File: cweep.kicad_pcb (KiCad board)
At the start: 2 copper layers, 108 x 82.5 mm, 73 parts, among them J1 24AWG Hole, J2 24AWG Hole, SW1 SW_Push, SW10 SW_Push, SW11 SW_Push, SW12 SW_Push, SW13 SW_Push, SW14 SW_Push, SW15 SW_Push, SW16 SW_Push, SW17 SW_Push, SW18 SW_SPST, SW19 SW_Omron_B3FS, SW2 SW_Push, SW3 SW_Push, SW4 SW_Push, SW5 SW_Push, SW6 SW_Push, SW7 SW_Push, SW8 SW_Push, SW9 SW_Push, U1 XIAO-nRF52840, U2 BQ25504RGTR

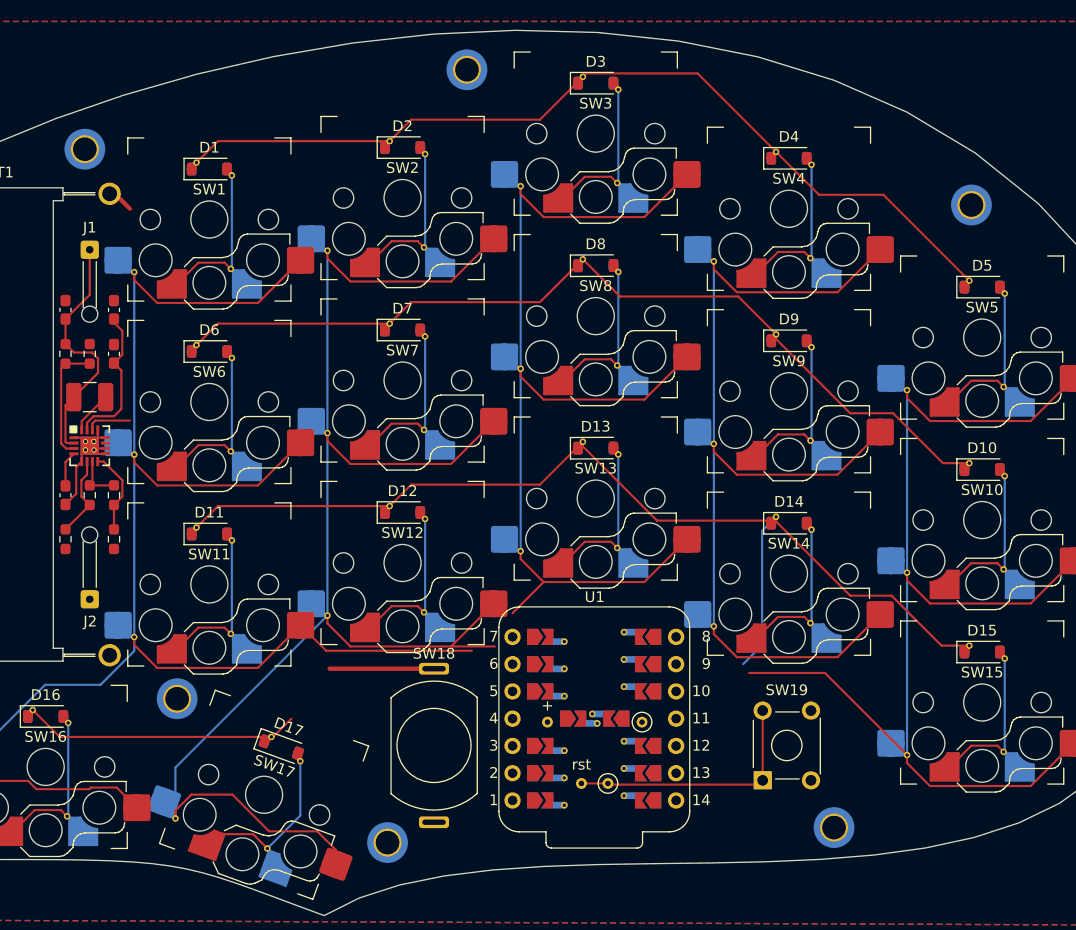
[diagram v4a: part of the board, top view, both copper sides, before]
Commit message: feat: make remaining components reversible
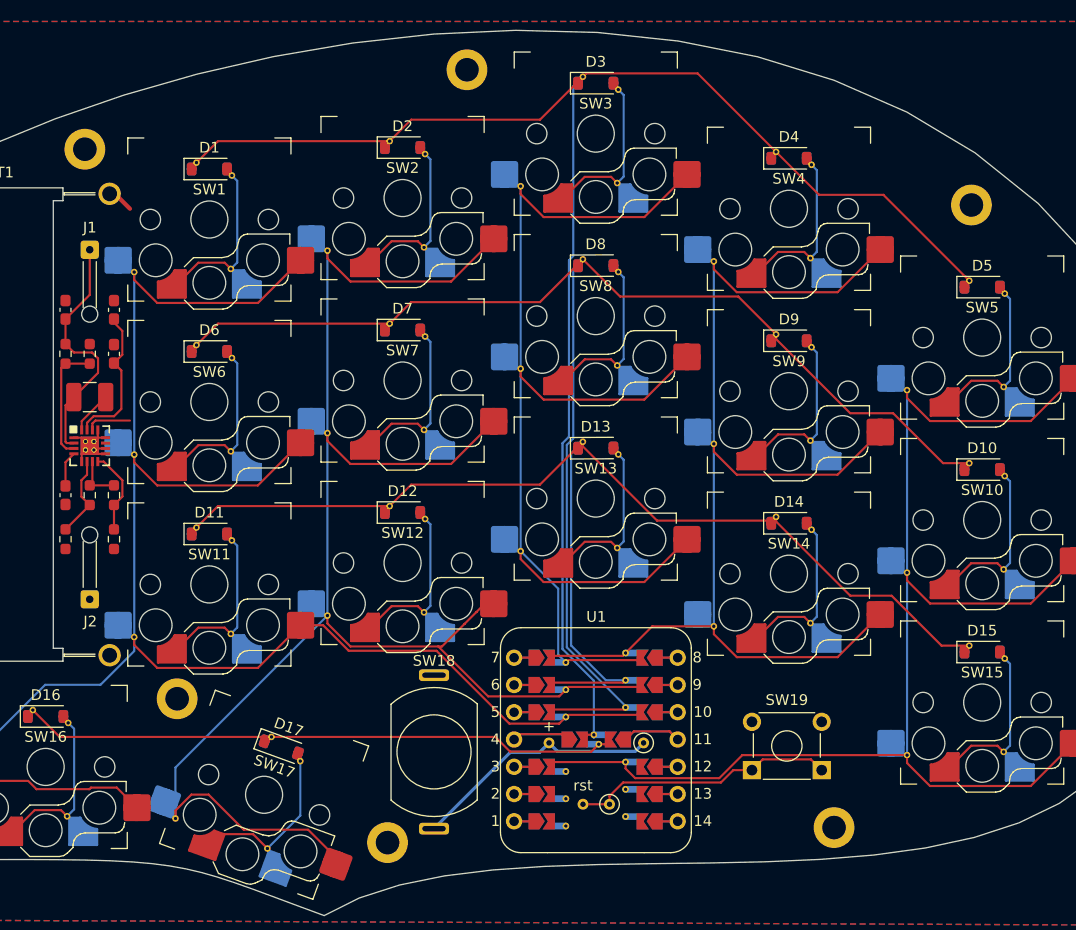
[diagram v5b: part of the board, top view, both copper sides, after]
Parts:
- BT1: footprint com_snapeda_Keystone:BatteryHolder_Keystone_230-1_1x10440 -> cweep:BatteryHolder_Keystone_230-1_1x10440
- H1, H2, H3, H4, H5, H6: footprint MountingHole:MountingHole_2.2mm_M2_DIN965_Pad_TopOnly -> cweep:MountingHole_2.2mm_M2_DIN965_Pad
- SW18: footprint KAN-15:SW_KAN-15_PHT -> cweep:SW_KAN-15_PHT_Reversible
- SW19: footprint Button_Switch_THT:SW_TH_Tactile_Omron_B3F-10xx -> cweep:SW_TH_Tactile_Omron_B3F-10xx_Reversible
- U1: footprint Seeed Studio XIAO Series Library:XIAO-nRF52840 -> cweep:XIAO-nRF52840_Reversible
- moved SW19 3.91 mm to (92.2, 79.7), turned to 0 degrees
- moved JP11 1.95 mm to (72.4, 79.0)
- moved JP4 1.95 mm to (76.5, 79.0)
- moved JP1 1.95 mm to (79.4, 86.7)
- moved JP2 1.95 mm to (79.4, 84.1)
- moved JP3 1.95 mm to (79.4, 81.6)
- moved JP5 1.95 mm to (79.4, 76.5)
- moved JP6 1.95 mm to (79.4, 74.0)
- moved JP7 1.95 mm to (79.4, 71.4)
- moved JP10 1.95 mm to (69.4, 76.5)
- moved JP12 1.95 mm to (69.4, 81.6)
- moved JP13 1.95 mm to (69.4, 84.1)
- moved JP14 1.95 mm to (69.4, 86.7)
- moved JP8 1.95 mm to (69.4, 71.4)
- moved JP9 1.95 mm to (69.4, 74.0)
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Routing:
- net /ROW0: track 83.4 -> 148.3 mm
- net /ROW1: track 83.4 -> 135.3 mm
- net /ROW3: track 25.8 -> 55.9 mm
- net /BAT: track 0.00 -> 23.5 mm
- net /COL0: track 152.8 -> 171.9 mm
- net /ROW2: track 99.0 -> 117.1 mm
- net /COL4: track 108.2 -> 125.7 mm
- net /COL1: track 138.9 -> 155.8 mm
- net /COL3: track 90.3 -> 106.8 mm
- net /COL2: track 94.4 -> 109.7 mm
- net /PIN4: track 0.00 -> 10.9 mm
- net /PIN11: track 0.00 -> 10.7 mm
- net /VBAT: track 16.6 -> 6.88 mm
- net GND: track 11.5 -> 6.88 mm
- net /PIN2: track 0.00 -> 3.77 mm
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
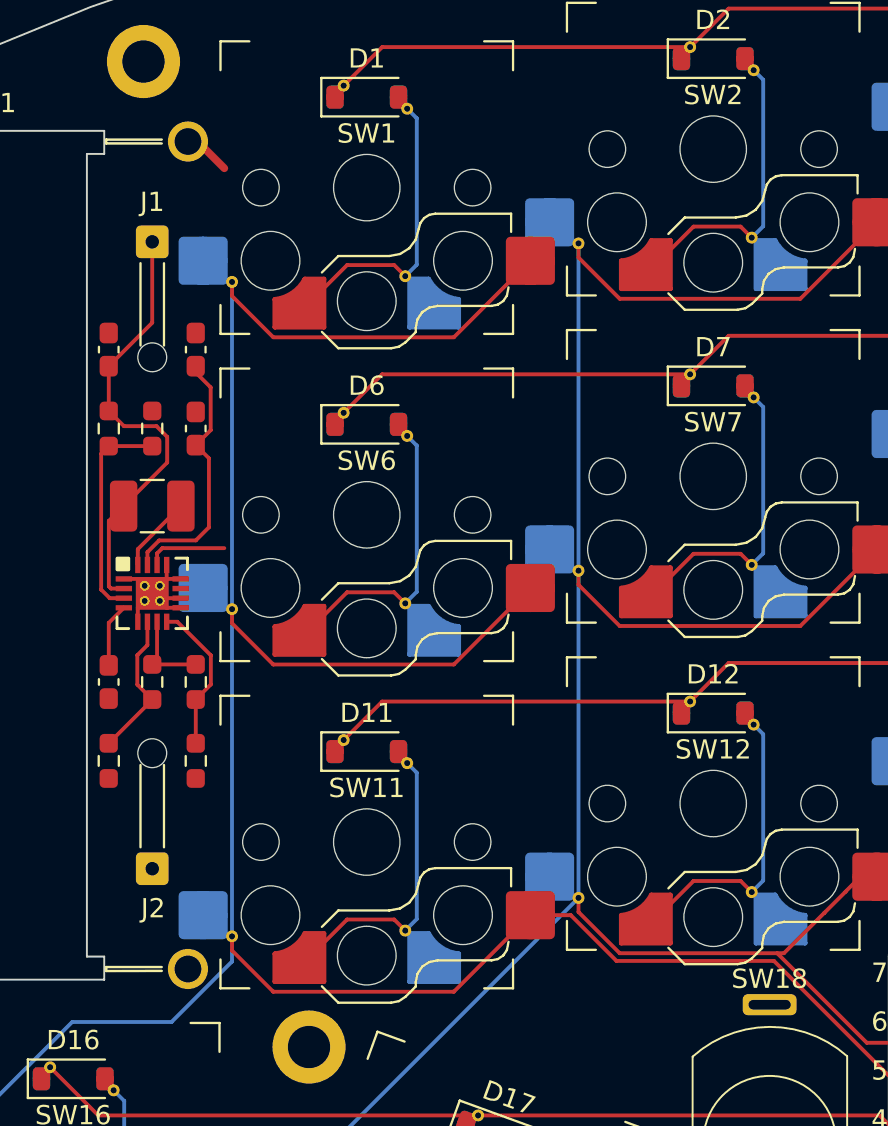
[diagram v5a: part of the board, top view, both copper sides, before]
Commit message: refactor: use kicad libraries for BQ25504
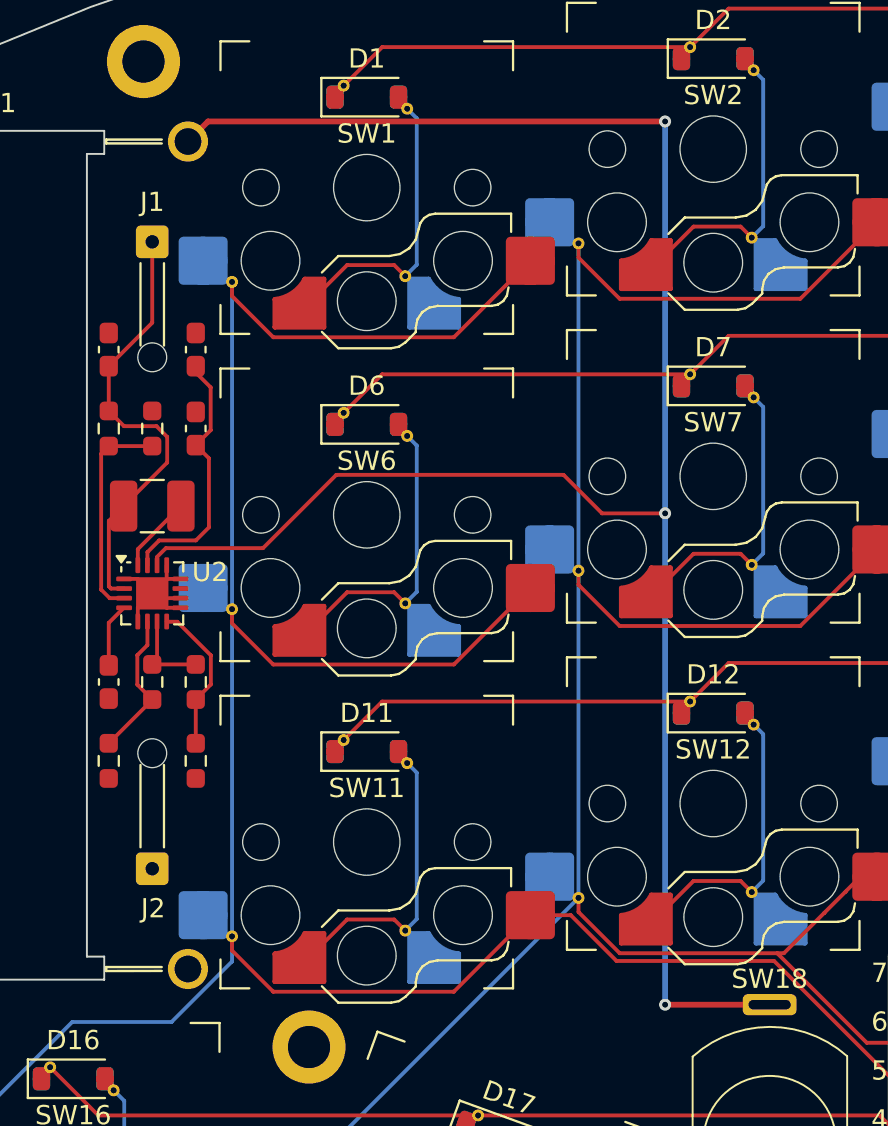
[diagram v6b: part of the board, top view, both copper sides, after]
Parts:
- U2: value BQ25504RGTR -> BQ25504; footprint BQ25504RGTR:RGT16_1P7X1P7 -> Package_DFN_QFN:VQFN-16-1EP_3x3mm_P0.5mm_EP1.68x1.68mm
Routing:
- net /VBAT: track 6.88 -> 106.0 mm, vias 0 -> 3

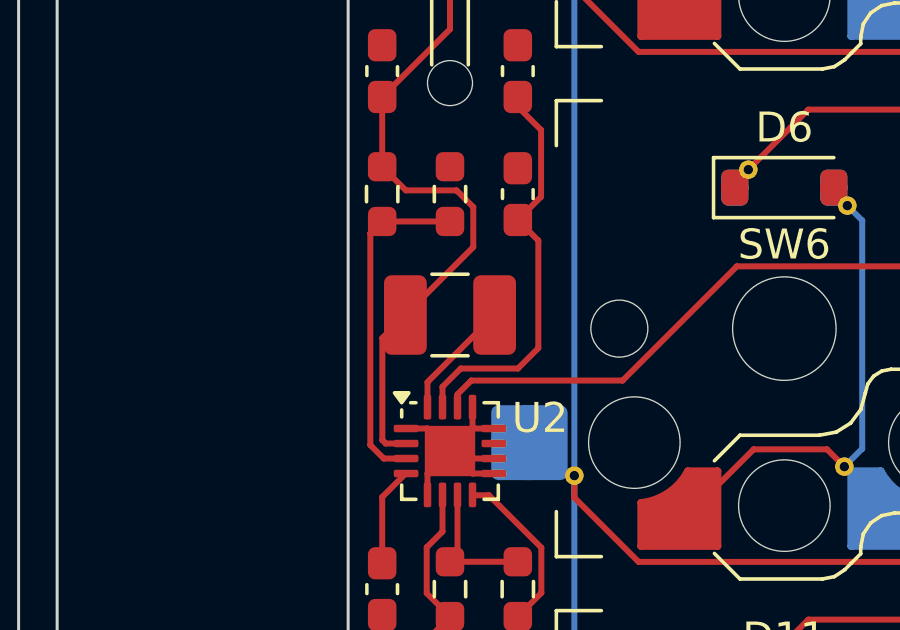
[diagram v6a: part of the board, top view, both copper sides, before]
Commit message: feat: add reversible inductor
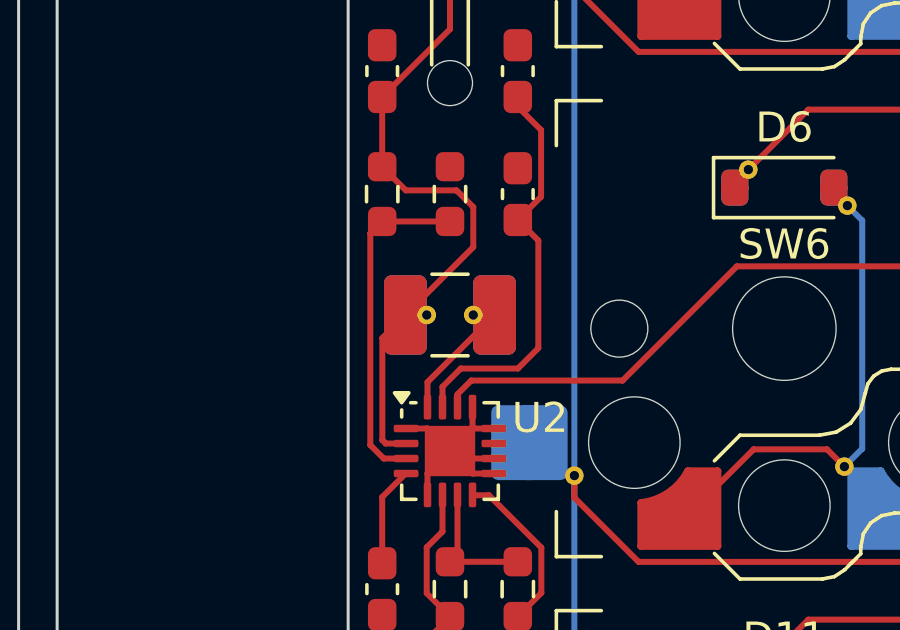
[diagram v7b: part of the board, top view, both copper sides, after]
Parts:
- LBST1: footprint Inductor_SMD:L_1210_3225Metric_Pad1.42x2.65mm_HandSolder -> cweep:L_1210_3225Metric_Pad1.42x2.65mm_HandSolder_Reversible
